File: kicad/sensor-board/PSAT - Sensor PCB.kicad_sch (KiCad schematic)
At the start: 55 parts, among them J1 533980471, J2 533980471, J3 533980471, J4 533980471, Q1 2N2222A, U1 ESP32-CAM, U2 CD-PA1616D, U3 BME280, U4 ADXL345, U5 ADXL375

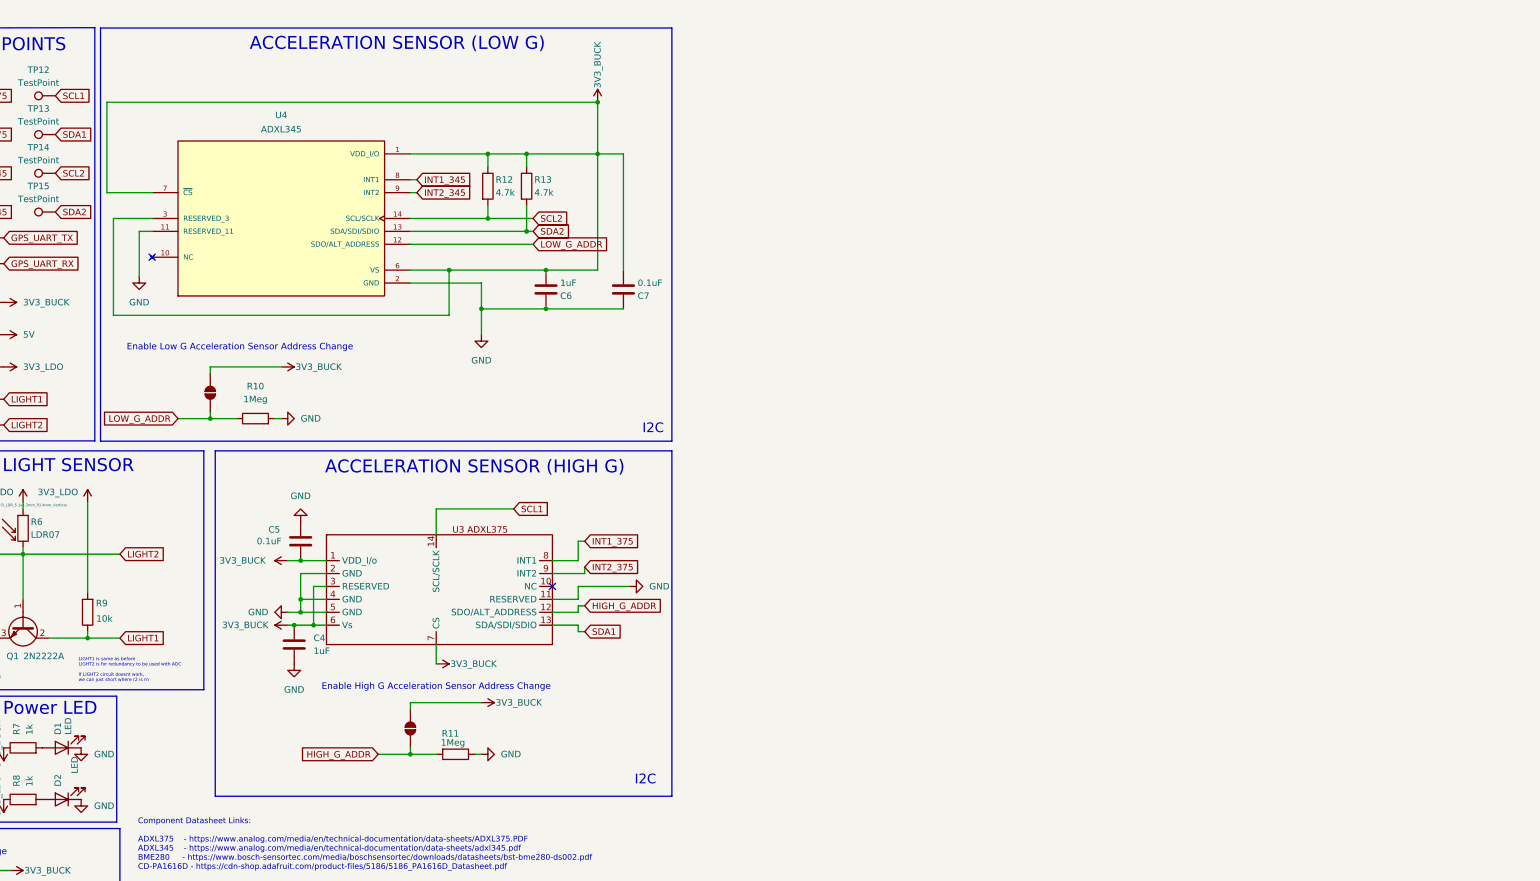
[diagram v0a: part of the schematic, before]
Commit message: feat: Gps changed to BMI323
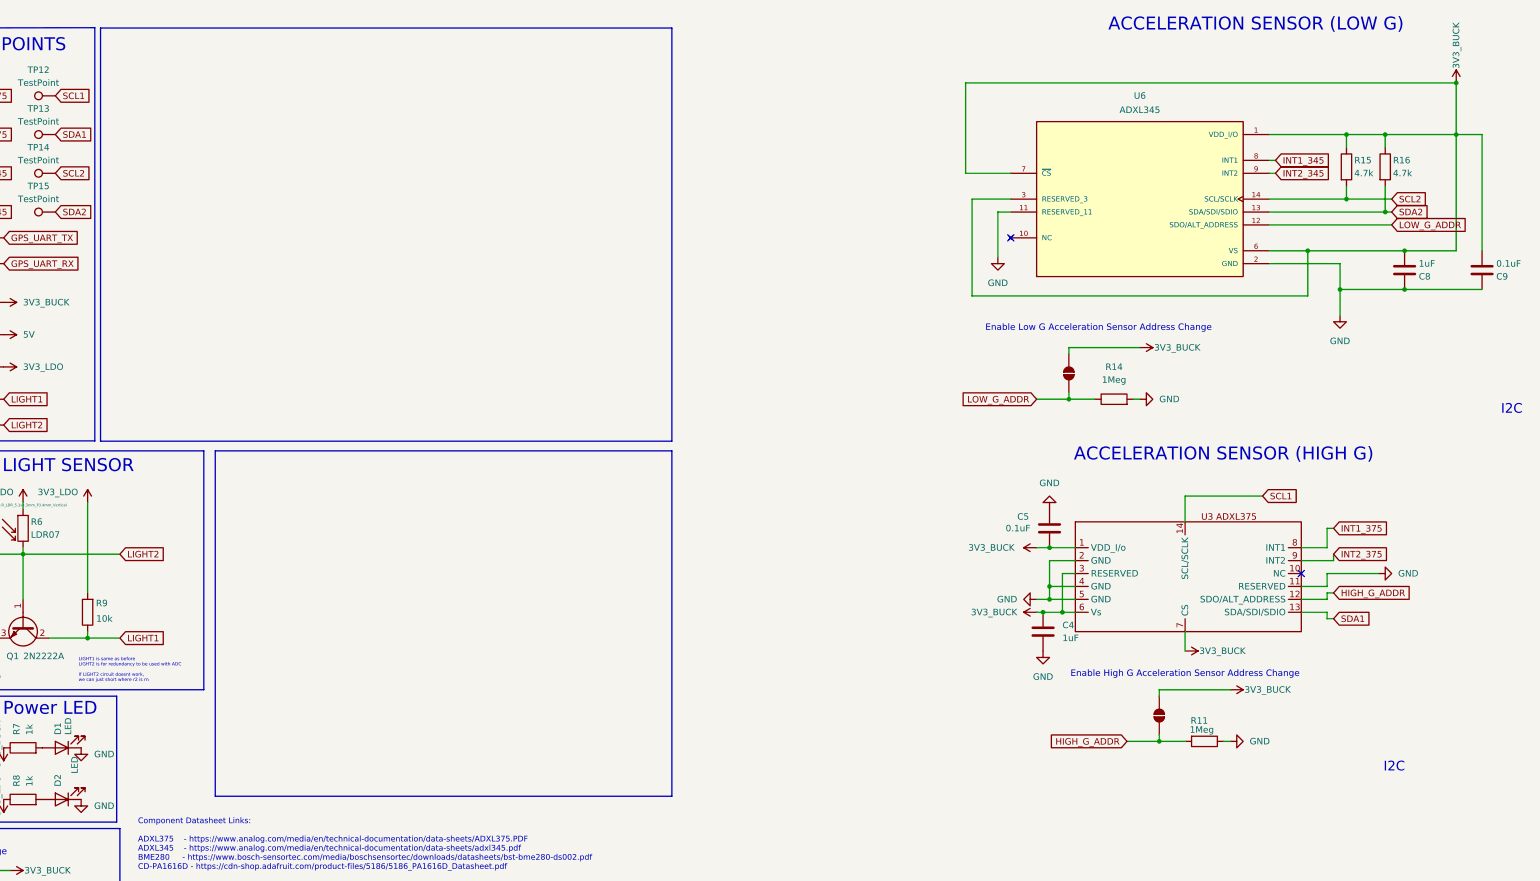
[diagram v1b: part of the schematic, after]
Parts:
- removed C6: 1uF, Capacitor_SMD:C_0805_2012Metric_Pad1.18x1.45mm_HandSolder, symbol Device:C
- removed C7: 0.1uF, Capacitor_SMD:C_0805_2012Metric_Pad1.18x1.45mm_HandSolder, symbol Device:C
- removed JP4: EN_5, Jumper:SolderJumper-2_P1.3mm_Open_Pad1.0x1.5mm, symbol Jumper:SolderJumper_2_Open
- removed R10: 1Meg, Resistor_SMD:R_0805_2012Metric_Pad1.20x1.40mm_HandSolder, symbol Device:R
- removed R12, R13: 4.7k, Resistor_SMD:R_0805_2012Metric_Pad1.20x1.40mm_HandSolder, symbol Device:R
- removed U4: ADXL345, ADXL345:adxl345, symbol adxl345:ADXL345
- added C8: 1uF, Capacitor_SMD:C_0805_2012Metric_Pad1.18x1.45mm_HandSolder, symbol Device:C
- added C9: 0.1uF, Capacitor_SMD:C_0805_2012Metric_Pad1.18x1.45mm_HandSolder, symbol Device:C
- added JP6: EN_5, Jumper:SolderJumper-2_P1.3mm_Open_Pad1.0x1.5mm, symbol Jumper:SolderJumper_2_Open
- added R14: 1Meg, Resistor_SMD:R_0805_2012Metric_Pad1.20x1.40mm_HandSolder, symbol Device:R
- added R15, R16: 4.7k, Resistor_SMD:R_0805_2012Metric_Pad1.20x1.40mm_HandSolder, symbol Device:R
- added U6: ADXL345, ADXL345:adxl345, symbol adxl345:ADXL345
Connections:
- net 3V3_BUCK: now also C8.1, C9.1, JP6.1 (A), R15.1, R16.1, U6.1 (VDD_I/O), U6.3 (RESERVED_3), U6.6 (VS), U6.7 (~{CS})
- net GND: now also C8.2, C9.2, R14.2, U6.11 (RESERVED_11), U6.2 (GND), U6.4 (GND), U6.5 (GND)
- net INT1_345: now also U6.8 (INT1)
- net INT2_345: now also U6.9 (INT2)
- net LOW_G_ADDR: now also JP6.2 (B), R14.1, U6.12 (SDO/ALT_ADDRESS)
- net SCL2: now also R15.2, U6.14 (SCL/SCLK)
- net SDA2: now also R16.2, U6.13 (SDA/SDI/SDIO)
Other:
- moved on the sheet: C4, C5, R11

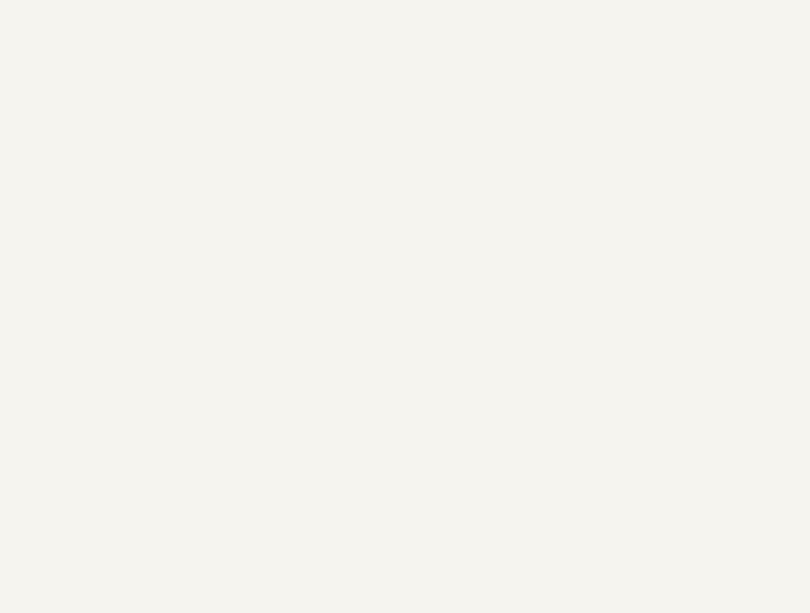
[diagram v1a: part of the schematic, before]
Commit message: feat: configured I2C connection for BMI323
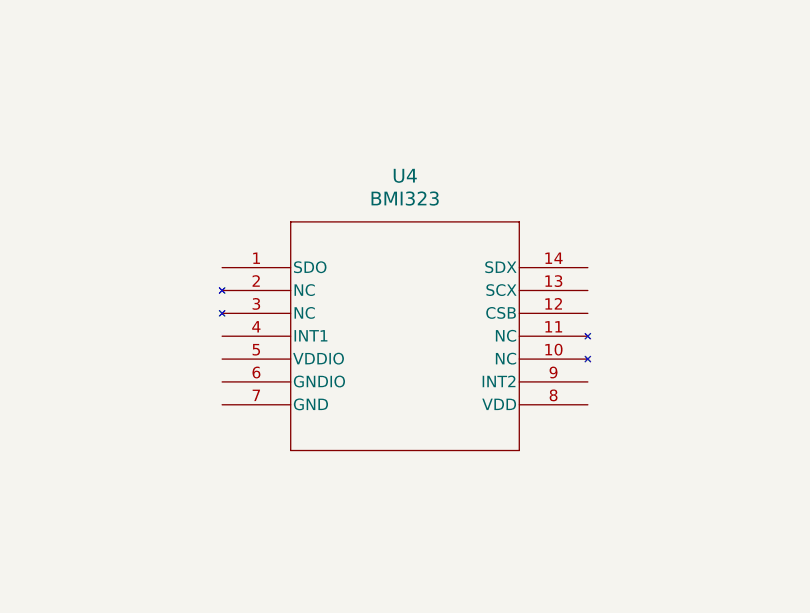
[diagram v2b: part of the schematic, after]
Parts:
- added U4: BMI323, BMI323:BMI323_BOS, symbol 2026-01-29_08-52-09:BMI323
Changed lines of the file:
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@@
+	)
+	(symbol
+		(lib_id "2026-01-29_08-52-09:BMI323")
+		(at 205.74 45.72 0)
+		(unit 1)
+		(exclude_from_sim no)
+		(in_bom yes)
+		(on_board yes)
+		(dnp no)
+		(fields_autoplaced yes)
+		(property "Reference" "U4"
+			(at 226.06 35.56 0)
+			(effects
+				(font
+					(size 1.524 1.524)
+				)
+			)
+		)
+		(property "Value" "BMI323"
+			(at 226.06 38.1 0)
+			(effects
+				(font
+					(size 1.524 1.524)
+				)
+			)
+		)
+		(property "Footprint" "BMI323:BMI323_BOS"
+			(at 205.74 45.72 0)
+			(effects
+				(font
+					(size 1.27 1.27)
+					(italic yes)
+				)
+				(hide yes)
+			)
+		)
+		(property "Datasheet" "BMI323"
+			(at 205.74 45.72 0)
+			(effects
+				(font
+					(size 1.27 1.27)
+					(italic yes)
+				)
+				(hide yes)
+			)
+		)
+		(property "Description" ""
+			(at 205.74 45.72 0)
+			(effects
+				(font
+					(size 1.27 1.27)
+				)
+				(hide yes)
+			)
+		)
+		(pin "14"
+		)
+		(pin "5"
+		)
+		(pin "7"
+		)
+		(pin "4"
+		)
+		(pin "13"
+		)
+		(pin "10"
+		)
+		(pin "1"
+		)
+		(pin "3"
+		)
+		(pin "12"
+		)
+		(pin "11"
+		)
+		(pin "9"
+		)
+		(pin "2"
+		)
+		(pin "6"
+		)
+		(pin "8"
+		)
+		(instances
+			(project ""
+				(path "/4cbf6b5d-7ed3-4842-986c-5d7275bd15b0"
+					(reference "U4")
+					(unit 1)
+				)
+			)
+		)
 	)
 	(symbol
